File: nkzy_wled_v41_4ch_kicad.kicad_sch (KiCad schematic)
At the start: 60 parts, among them CN1 1x3P_3.96mm_RA_Conn, CN2 1x3P_3.96mm_RA_Conn, CN3 1x3P_3.96mm_RA_Conn, CN4 1x3P_3.96mm_RA_Conn, CN5 1x2P_3.96mm_RA_Conn, J1 1x2P_2.54mm_RA_Conn, J2 HC-2510-3AW, K1 12VDC_SPDT, Q1 AO3401, U1 ESP32-WROOM-32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

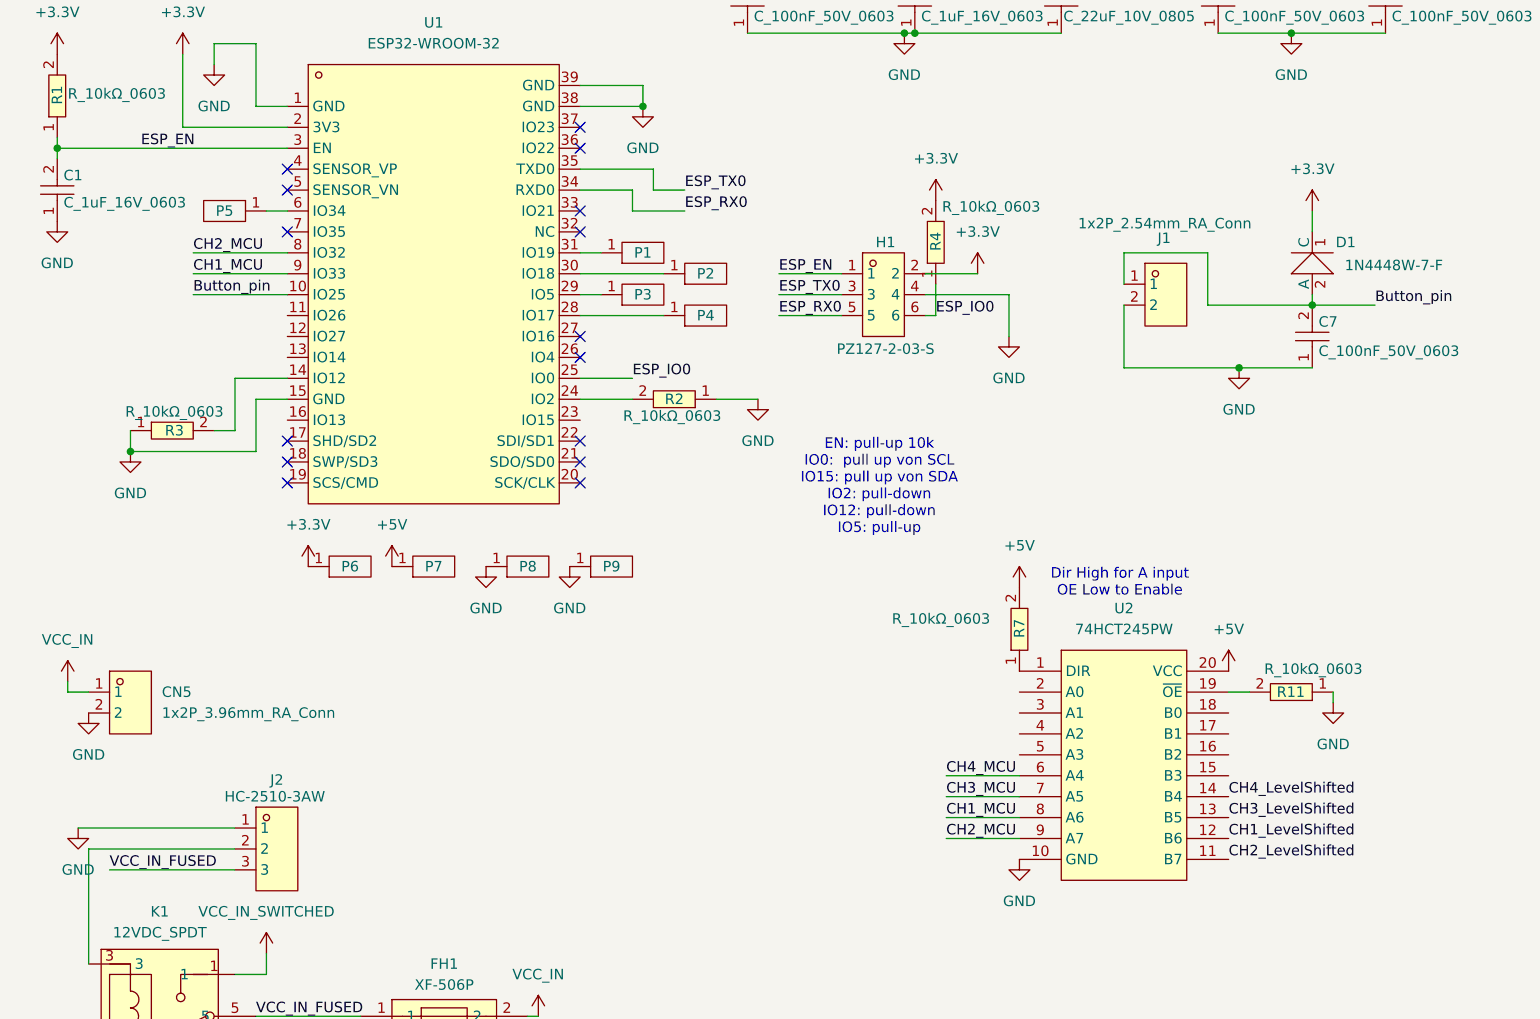
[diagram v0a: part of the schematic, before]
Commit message: Routed 4 ch pcb and resolved all DRC
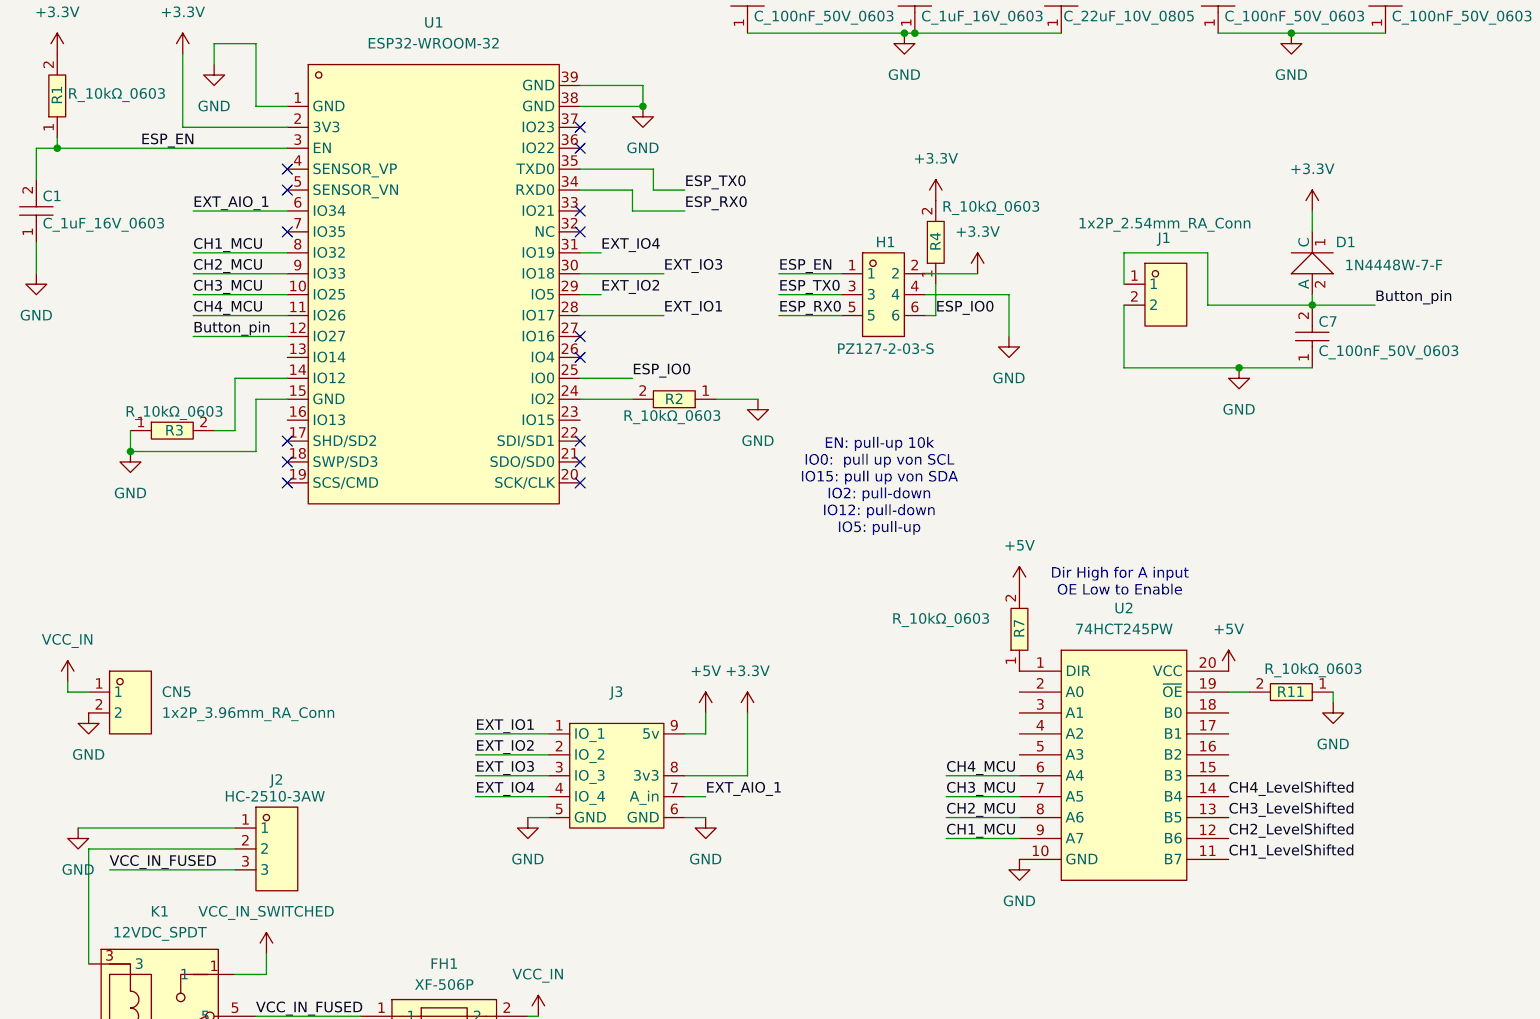
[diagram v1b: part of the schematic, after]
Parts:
- removed P1, P2, P3, P4, P5, P6, P7, P8, P9: ~, nkzy_wled_lib:Pad_2.5x1mm, symbol nkzy_wled_lib:PAD_Standalone
- added J3: ~, nkzy_wled_lib:nkzy_addon_footprint, symbol nkzy_wled_lib:nkzy_addon_pins
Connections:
- net +3.3V: now also J3.8 (3v3)
- net +5V: now also J3.9 (5v)
- net Button_pin: now also U1.12 (IO27); no longer U1.10 (IO25)
- net CH1_LevelShifted: now also U2.11 (B7); no longer U2.12 (B6)
- net CH1_MCU: now also U1.8 (IO32), U2.9 (A7); no longer U1.9 (IO33), U2.8 (A6)
- net CH2_LevelShifted: now also U2.12 (B6); no longer U2.11 (B7)
- net CH2_MCU: now also U1.9 (IO33), U2.8 (A6); no longer U1.8 (IO32), U2.9 (A7)
- net CH3_MCU: now also U1.10 (IO25)
- net CH4_MCU: now also U1.11 (IO26)
- net GND: now also J3.5 (GND), J3.6 (GND)
- net EXT_IO4: now reaches U1.31 (IO19)
- net EXT_IO4: now also J3.4 (IO_4)
- net EXT_IO3: now reaches U1.30 (IO18)
- net EXT_IO3: now also J3.3 (IO_3)
- net EXT_IO1: now reaches U1.28 (IO17)
- net EXT_IO1: now also J3.1 (IO_1)
- net EXT_IO2: now reaches U1.29 (IO5)
- net EXT_IO2: now also J3.2 (IO_2)
- net EXT_AIO_1: now reaches U1.6 (IO34)
- net EXT_AIO_1: now also J3.7 (A_in)
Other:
- moved on the sheet: C1
